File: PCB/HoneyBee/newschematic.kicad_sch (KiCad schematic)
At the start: 43 parts, among them J1 S2B-PH-K-SLFSN, J2 10104110-0001LF, M1 Motor_DC, M2 Motor_DC, M3 Motor_DC, M4 Motor_DC, M5 Motor_DC, M6 Motor_DC, Q1 IRLML2502TRPbF, Q2 IRLML2502TRPbF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

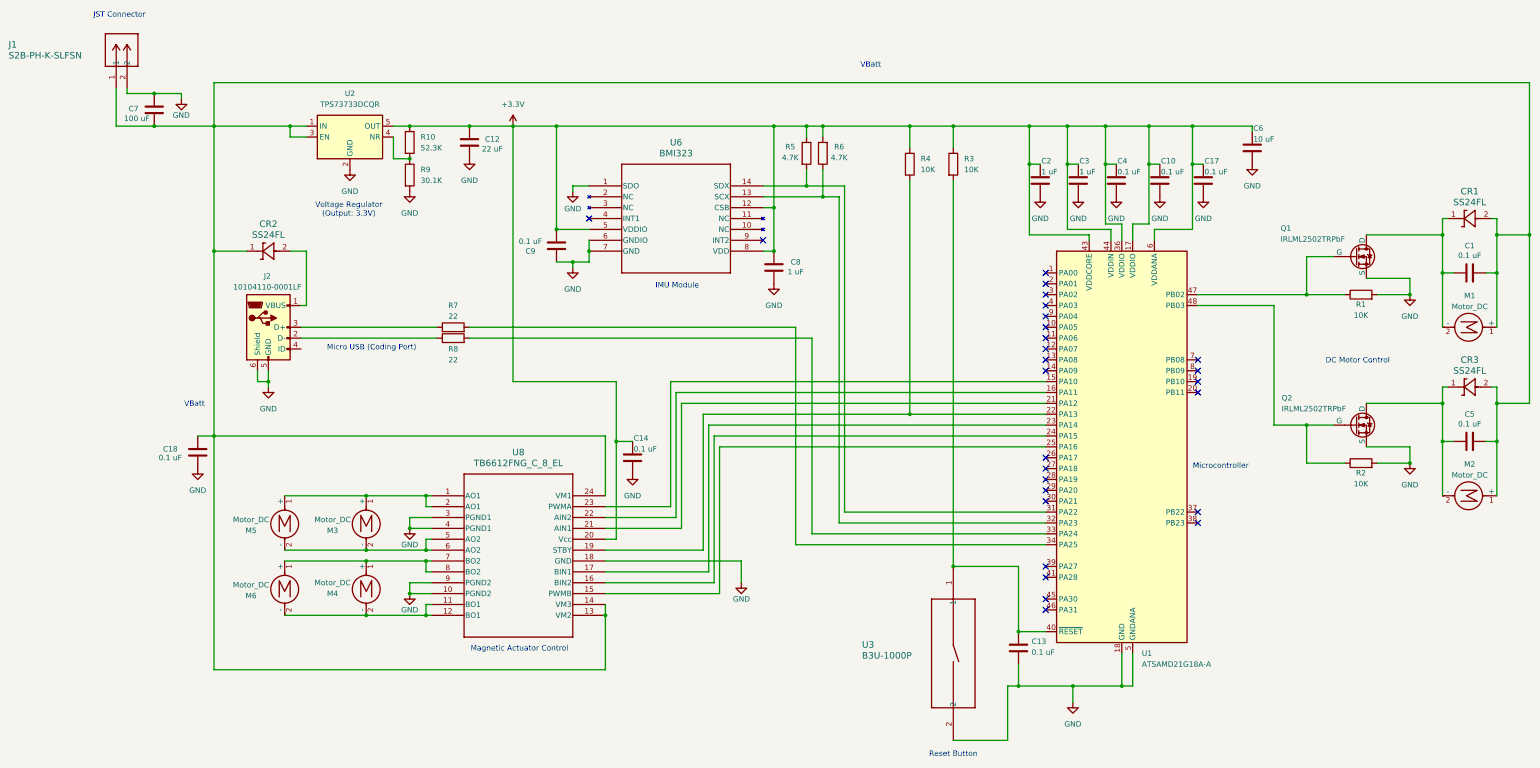
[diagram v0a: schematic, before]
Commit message: PCB Draft 1-Minimal Wiring
Still adjusting location of components.
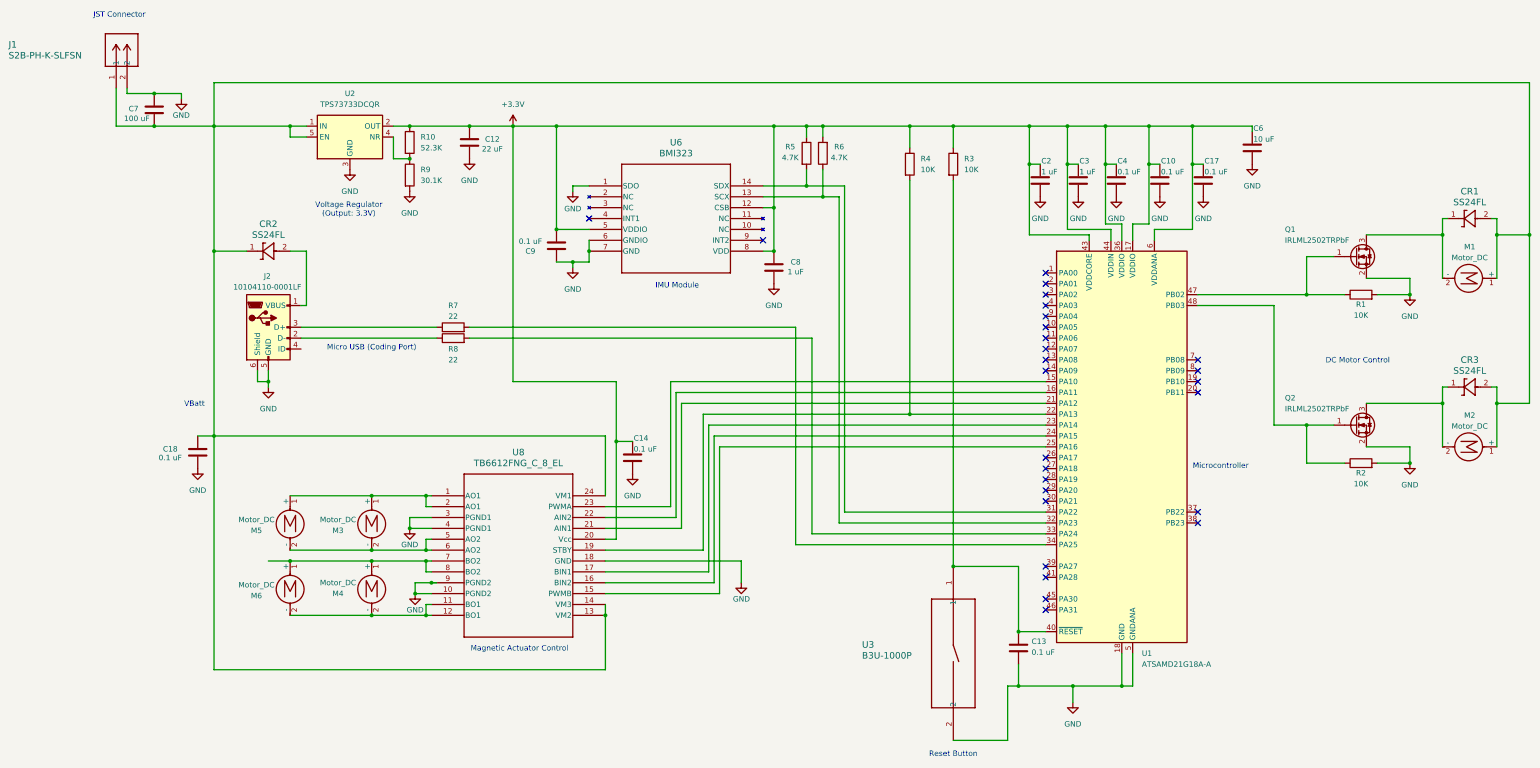
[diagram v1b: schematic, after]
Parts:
- removed C1, C5: 0.1 uF, Capacitor_SMD:C_0603_1608Metric_Pad1.08x0.95mm_HandSolder, symbol Device:C
- removed Q1, Q2: IRLML2502TRPbF, Package_TO_SOT_SMD:SOT-23W_Handsoldering, symbol Simulation_SPICE:NMOS
- added Q1, Q2: IRLML2502TRPbF, Package_TO_SOT_SMD:SOT-23W_Handsoldering, symbol Transistor_FET:Q_NMOS_GSD
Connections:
- net +3.3V: now also U2.2 (OUT); no longer U2.5 (OUT)
- net GND: now also U2.3 (GND), Q1.2 (S), Q2.2 (S); no longer U2.2 (GND)
- net at C18.1, C7.1, CR1.2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: now also U2.5 (EN); no longer U2.3 (EN)
- net at R1.1, U1.47 (PB02): now also Q1.1 (G)
- net at R2.1, U1.48 (PB03): now also Q2.1 (G)
- net at CR3.1, M2.2 (-): now also Q2.3 (D)
- net at CR1.1, M1.2 (-): now also Q1.3 (D)
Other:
- moved on the sheet: M1, M2, M3, M4, M5, M6
